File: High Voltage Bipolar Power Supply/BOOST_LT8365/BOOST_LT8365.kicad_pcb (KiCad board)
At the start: 2 copper layers, 41 parts, among them J3 1715721, U1 LT8365, U3 LT8365

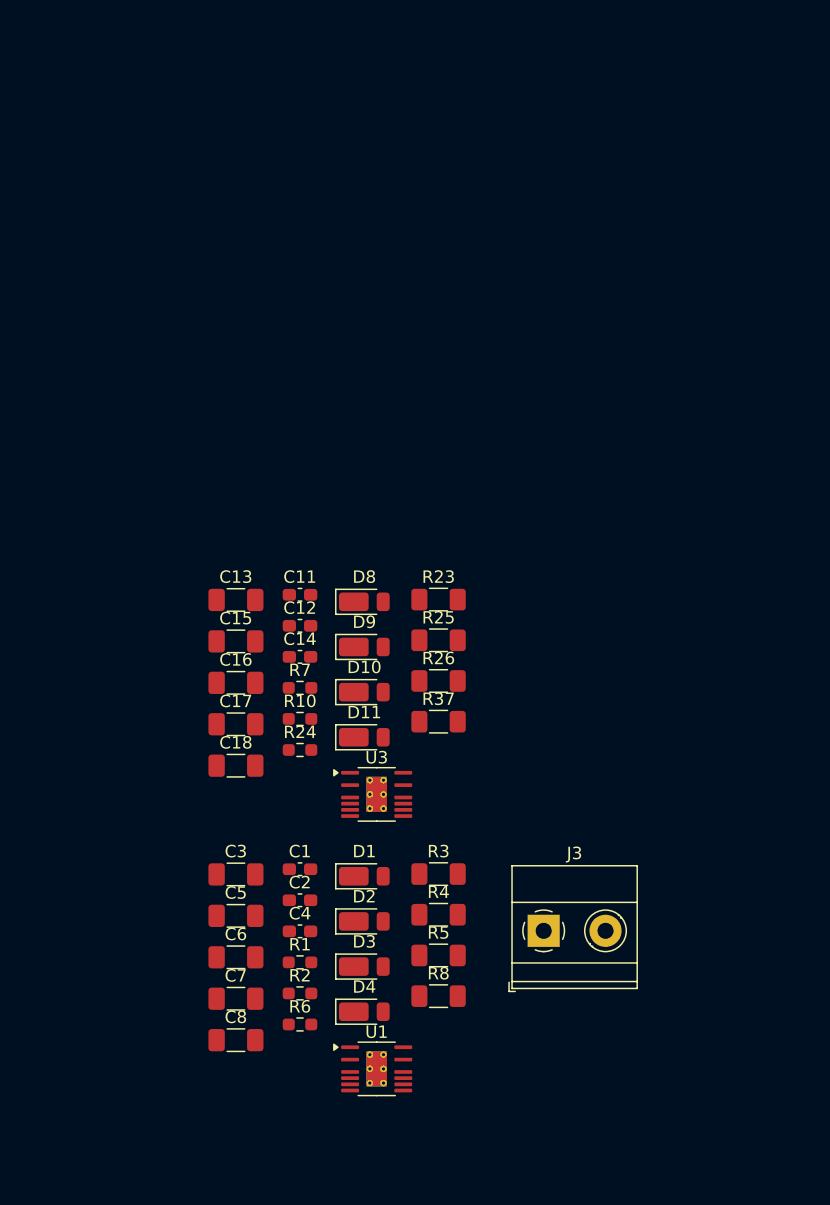
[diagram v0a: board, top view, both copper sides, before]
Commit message: BOOST_LT8365 : PCB layout
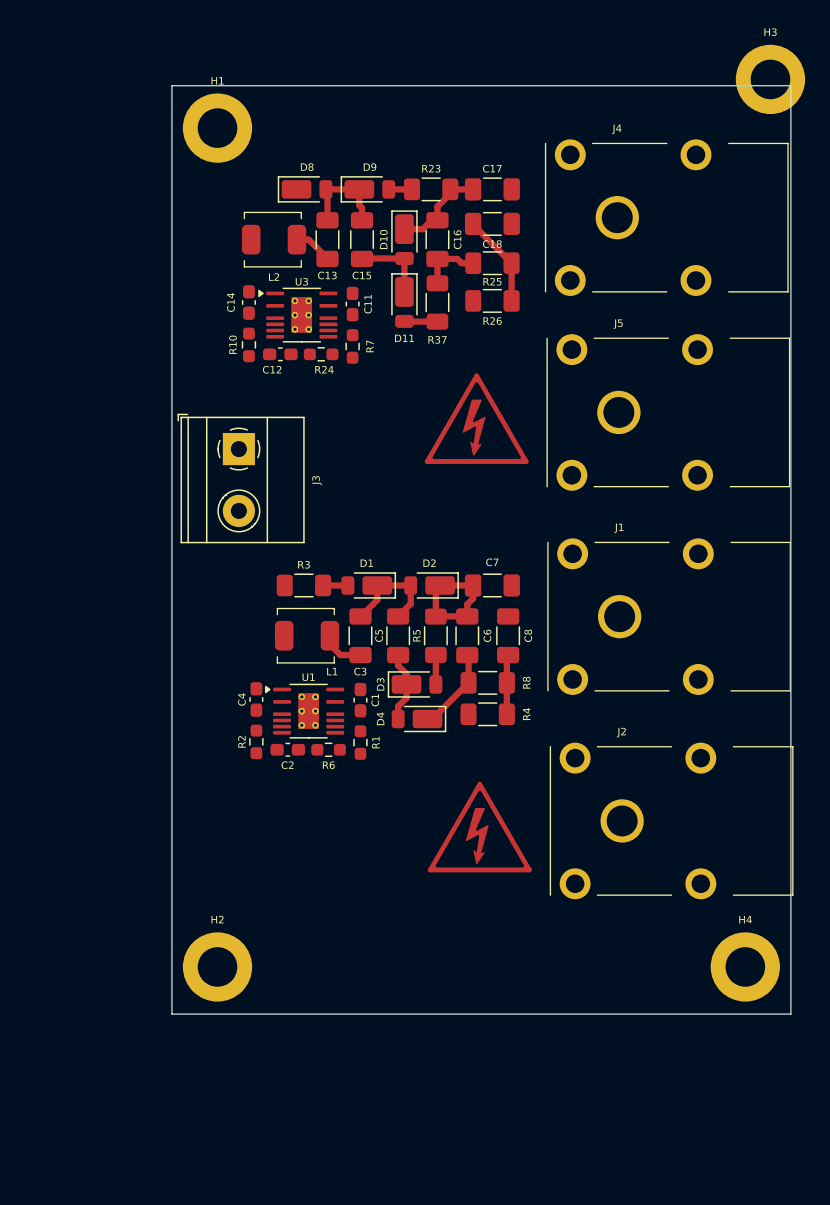
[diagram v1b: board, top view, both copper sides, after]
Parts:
- added H1: MountingHole, MountingHole:MountingHole_3.2mm_M3_DIN965_Pad, F.Cu at (138.7, 45.0)
- added H2: MountingHole, MountingHole:MountingHole_3.2mm_M3_DIN965_Pad, F.Cu at (138.7, 112.8)
- added H3: MountingHole, MountingHole:MountingHole_3.2mm_M3_DIN965_Pad, F.Cu at (183.4, 41.0)
- added H4: MountingHole, MountingHole:MountingHole_3.2mm_M3_DIN965_Pad, F.Cu at (181.4, 112.8)
- added J1: FCR7350R, BOOST_LT8365:S16N-PC, F.Cu at (171.2, 84.5)
- added J2: FCR7350B, BOOST_LT8365:S16N-PC, F.Cu at (171.4, 101.0)
- added J4: FCR7350Y, BOOST_LT8365:S16N-PC, F.Cu at (171.0, 52.2)
- added J5: FCR7350B, BOOST_LT8365:S16N-PC, F.Cu at (171.1, 67.9)
- added L1: 74437324100, BOOST_LT8365:74437324100, F.Cu at (145.9, 86.0)
- added L2: 74437324100, BOOST_LT8365:74437324100, F.Cu at (143.3, 54.0)
- added SYM1: SYM_Flash_XLarge, Symbol:Symbol_HighVoltage_Triangle_8x7mm_Copper, F.Cu at (159.6, 68.5)
- added SYM2: SYM_Flash_XLarge, Symbol:Symbol_HighVoltage_Triangle_8x7mm_Copper, F.Cu at (159.9, 101.5)
- moved C18 48.5 mm to (160.9, 52.7)
- moved C17 48.0 mm to (160.9, 49.9)
- moved J3 46.1 mm to (140.4, 70.9), turned to -90 degrees
- moved C8 39.4 mm to (162.2, 86.0), turned to 90 degrees
- moved C16 39.4 mm to (156.5, 54.0), turned to 90 degrees
- moved C7 39.3 mm to (160.9, 81.9)
- moved U3 39.2 mm to (145.5, 60.1)
- moved D9 37.0 mm to (151.0, 49.9)
- moved D10 36.7 mm to (153.8, 54.0), turned to -90 degrees
- moved D11 35.3 mm to (153.8, 59.1), turned to -90 degrees
- moved C15 34.0 mm to (150.4, 54.0), turned to -90 degrees
- moved R37 33.9 mm to (156.5, 59.1), turned to 90 degrees
- moved D8 33.7 mm to (145.9, 49.9)
- moved R23 33.2 mm to (156.0, 49.9)
- moved R24 32.0 mm to (147.1, 63.2), turned to 180 degrees
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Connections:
- net Net-(C16-Pad1) renamed /Negative Voltage/-HV4
- net Net-(D1-K) renamed /Positive Voltage/+HV2
- net Net-(D10-A) renamed /Negative Voltage/-HV3
- net Net-(D3-K) renamed /Positive Voltage/+HV3
- net Net-(D4-K) renamed /Positive Voltage/+HV4
- net Net-(D8-A) renamed /Negative Voltage/-HV2
- net Net-(U1-SW1) renamed /Positive Voltage/+HV1
- net Net-(U3-SW1) renamed /Negative Voltage/-HV1
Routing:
- net Net-(D2-K): track 0.00 -> 10.6 mm
- net /Positive Voltage/+HV2: track 0.00 -> 8.71 mm
- net /Negative Voltage/-HV2: track 0.00 -> 7.85 mm
- net Net-(D10-K): track 0.00 -> 7.74 mm
- net -110V: track 0.00 -> 7.51 mm
- net /Positive Voltage/+HV4: track 0.00 -> 6.81 mm
- net /Negative Voltage/-HV3: track 0.00 -> 6.15 mm
- net /Positive Voltage/+HV3: track 0.00 -> 5.73 mm
- net /Negative Voltage/-HV4: track 0.00 -> 5.54 mm
- net +110V: track 0.00 -> 4.83 mm
- net /Positive Voltage/+HV1: track 0.00 -> 3.53 mm
- net /Negative Voltage/-HV1: track 0.00 -> 3.14 mm
- net Net-(D11-A): track 0.00 -> 2.68 mm
- net Net-(D3-A): track 0.00 -> 2.39 mm
- net Net-(D1-A): track 0.00 -> 2.00 mm
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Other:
- board outline added: 50 x 75.1 mm

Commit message: BOOST_LT8365 : PCB design done
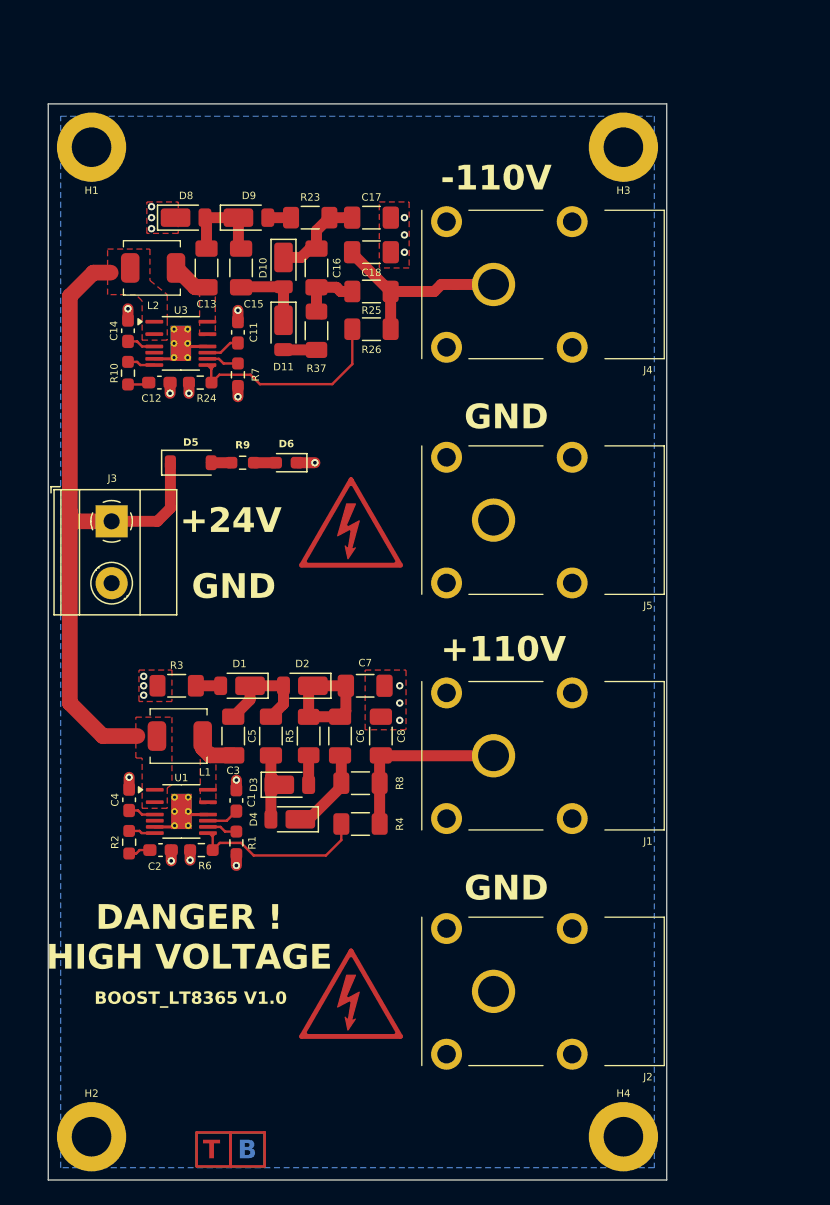
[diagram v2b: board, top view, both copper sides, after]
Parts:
- added D5: MMSZ5249B, Diode_SMD:D_SOD-123, F.Cu at (136.5, 72.0)
- added D6: RED, LED_SMD:LED_0603_1608Metric_Pad1.05x0.95mm_HandSolder, F.Cu at (144.2, 72.0)
- added R9: 370, Resistor_SMD:R_0603_1608Metric_Pad0.98x0.95mm_HandSolder, F.Cu at (140.7, 72.0)
- moved J2 17.3 mm to (161.0, 114.8)
- moved H2 17.1 mm to (128.5, 126.5)
- moved SYM2 17.0 mm to (149.5, 114.9)
- moved H4 16.9 mm to (171.5, 126.5)
- moved J1 15.2 mm to (161.0, 95.7)
- moved R4 13.6 mm to (150.2, 101.2)
- moved J5 13.4 mm to (161.0, 76.7)
- moved SYM1 13.2 mm to (149.5, 76.8)
- moved U1 13.1 mm to (135.8, 100.2)
- moved C3 13.1 mm to (140.0, 94.1)
- moved C6 13.1 mm to (148.6, 94.1)
- moved C8 13.1 mm to (151.9, 94.1)
- moved D1 13.1 mm to (140.5, 90.0)
- moved D2 13.1 mm to (145.5, 90.0)
- moved L1 13.1 mm to (135.6, 94.1)
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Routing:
- net +24V: track 0.00 -> 56.4 mm
- net GND: track 0.00 -> 20.0 mm, vias 0 -> 23
- net Net-(U3-FBX): track 0.00 -> 17.9 mm
- net Net-(U1-FBX): track 0.00 -> 14.6 mm
- net -110V: track 7.51 -> 18.6 mm
- net +110V: track 4.83 -> 14.8 mm
- net Net-(U3-SS): track 0.00 -> 2.79 mm
- net Net-(U3-RT): track 0.00 -> 2.62 mm
- net Net-(U1-SS): track 0.00 -> 2.62 mm
- net Net-(U1-RT): track 0.00 -> 2.45 mm
- net Net-(U3-INVTCC): track 0.00 -> 2.29 mm
- net Net-(U3-VC): track 0.00 -> 2.23 mm
- net Net-(U1-INVTCC): track 0.00 -> 2.21 mm
- net Net-(U1-VC): track 0.00 -> 2.15 mm
- net Net-(C2-Pad1): track 0.00 -> 1.79 mm
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- added copper zone on F.Cu, net +24V
- added copper zone on F.Cu, net /Negative Voltage/-HV1
- added copper zone on F.Cu, net /Positive Voltage/+HV1
- added copper zone on B.Cu, net GND
- added copper zone on F.Cu, net GND
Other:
- board size 50 x 75.1 mm -> 50 x 87 mm
- board text added: "+110V"
- board text added: "+24V"
- board text added: "-110V"
- board text added: "B"
- board text added: "BOOST_LT8365 V1.0"
- board text added: "DANGER ! HIGH VOLTAGE"
- board text added: "GND"
- board text added: "T"
